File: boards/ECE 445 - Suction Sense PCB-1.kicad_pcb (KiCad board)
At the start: 2 copper layers, 23 parts, among them J1 Paddle Sensor, J2 Motion Sensor, U1 ESP32-WROOM-32E, U2 TPS2120YFPR, U3 AP62150Z6

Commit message: routed
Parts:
- added J3: Battery Connector, Connector_PinSocket_2.00mm:PinSocket_1x02_P2.00mm_Vertical, F.Cu at (182.8, 126.4)
- added J4: Barrel_Jack, Connector_BarrelJack:BarrelJack_CUI_PJ-036AH-SMT_Horizontal, F.Cu at (177.3, 88.1)
- moved H4 85.4 mm to (102.2, 142.4)
- moved H1 72.2 mm to (102.2, 56.3)
- moved C1 67.8 mm to (168.4, 111.6)
- moved C2 65.0 mm to (161.2, 125.9)
- moved C3 63.8 mm to (155.3, 139.6)
- moved H3 54.7 mm to (185.4, 139.8)
- moved C5 32.7 mm to (128.8, 140.0)
- moved H2 24.4 mm to (182.2, 56.0)
- moved R7 23.9 mm to (122.7, 96.0)
- moved J1 19.6 mm to (103.1, 107.1)
- moved U2 18.5 mm to (152.6, 99.6)
- moved U1 14.7 mm to (143.9, 83.5)
- moved J2 13.1 mm to (108.7, 121.2)
- moved C4 12.7 mm to (106.9, 90.4)
- moved R3 12.0 mm to (122.6, 111.1)
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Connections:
- R7 pad 1: +12V -> +12VA
- U2 pad B1: +12V -> +12VA
- U2 pad B3: +12V -> +12VB
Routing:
- net GND: track 0.00 -> 288.4 mm, vias 0 -> 1
- net /3v3: track 0.00 -> 138.7 mm, vias 0 -> 2
- net +12VA: track 0.00 -> 84.3 mm, vias 0 -> 2
- net /EN: track 0.00 -> 82.2 mm, vias 0 -> 4
- net /IO35: track 0.00 -> 75.1 mm, vias 0 -> 2
- net /IO5: track 0.00 -> 55.6 mm, vias 0 -> 1
- net /IO12: track 0.00 -> 47.0 mm, vias 0 -> 1
- net Net-(U3-FB): track 0.00 -> 35.0 mm, vias 0 -> 2
- net Net-(R7-Pad2): track 0.00 -> 34.3 mm
- net Net-(U3-BST): track 0.00 -> 33.1 mm, vias 0 -> 2
- net Net-(R1-Pad2): track 0.00 -> 33.0 mm
- net /BUCK_IN: track 0.00 -> 31.1 mm
- net Net-(U3-SW): track 0.00 -> 29.1 mm, vias 0 -> 2
- net +12VB: track 0.00 -> 18.0 mm, vias 0 -> 1

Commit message: adding changes to the pcb finishing connections with power mux
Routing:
- net GND: track 288.4 -> 318.3 mm, vias 1 -> 3
- net /BUCK_IN: track 31.1 -> 58.8 mm, vias 0 -> 1
- net +12VB: track 18.0 -> 36.4 mm
- net +12VA: track 84.3 -> 93.1 mm
- net /IO2: track 0.00 -> 7.30 mm
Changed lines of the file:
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@@
 	(segment
 		(start 144.5483 112.9453)
-		(end 144.5483 122.1517)
+		(end 144.5483 115.3)
 		(width 0.2)
 		(layer "F.Cu")
@@
 	)
 	(segment
+		(start 144.5483 115.3)
+		(end 144.5483 122.1517)
+		(width 0.2)
+		(layer "F.Cu")
+		(net 2)
+	)
+	(segment
 		(start 173.9937 123.9503)
 		(end 158.371 139.573)
@@
 	)
 	(segment
+		(start 157.7 108.3)
+		(end 157.7 104.943997)
+		(width 0.2)
+		(layer "F.Cu")
+		(net 2)
+	)
+	(segment
+		(start 144.5483 115.3)
+		(end 144.6096 115.3)
+		(width 0.2)
+		(layer "F.Cu")
+		(net 2)
+	)
+	(segment
 		(start 150.8386 75.2141)
 		(end 151.5653 75.2141)
@@
 	)
 	(segment
+		(start 157.7 104.943997)
+		(end 153.178002 100.421999)
+		(width 0.2)
+		(layer "F.Cu")
+		(net 2)
+	)
+	(segment
 		(start 109.984 90.424)
 		(end 105.664 94.744)
@@
 		(net 2)
 	)
+	(via
+		(at 144.6096 115.3)
+		(size 0.6)
+		(drill 0.3)
+		(layers "F.Cu" "B.Cu")
+		(net 2)
+	)
+	(via
+		(at 157.7 108.3)
+		(size 0.6)
+		(drill 0.3)
+		(layers "F.Cu" "B.Cu")
+		(net 2)
+	)
 	(segment
 		(start 144.9615 84.8285)
@@
 	)
 	(segment
+		(start 150.1 115.3)
+		(end 150.1 110.6)
+		(width 0.2)
+		(layer "B.Cu")
+		(net 2)
+	)
+	(segment
 		(start 141.667 82.934)
 		(end 143.067 82.934)
@@
 	)
 	(segment
+		(start 157.7 110.6)
+		(end 157.7 108.3)
+		(width 0.2)
+		(layer "B.Cu")
+		(net 2)
+	)
+	(segment
 		(start 143.067 81.534)
 		(end 141.667 81.534)
@@
 	)
 	(segment
+		(start 144.6096 115.3)
+		(end 150.1 115.3)
+		(width 0.2)
+		(layer "B.Cu")
+		(net 2)
+	)
+	(segment
+		(start 150.1 110.6)
+		(end 157.7 110.6)
+		(width 0.2)
+		(layer "B.Cu")
+		(net 2)
+	)
+	(segment
 		(start 143.767 83.634)
 		(end 144.9615 84.8285)
@@
 	(segment
 		(start 145.2096 132.5116)
-		(end 145.2096 112.197)
+		(end 145.2096 116.7)
 		(width 0.2)
 		(layer "F.Cu")
@@
 	)
 	(segment
+		(start 151.7 110.6)
+		(end 151.7 106.8827)
+		(width 0.2)
+		(layer "F.Cu")
+		(net 5)
+	)
+	(segment
+		(start 145.2096 116.7)
+		(end 152.6 116.7)
+		(width 0.2)
+		(layer "F.Cu")
+		(net 5)
+	)
+	(segment
+		(start 155.2 114.1)
+		(end 151.7 110.6)
+		(width 0.2)
+		(layer "F.Cu")
+		(net 5)
+	)
+	(segment
+		(start 152.6 116.7)
+		(end 155.2 114.1)
+		(width 0.2)
+		(layer "F.Cu")
+		(net 5)
+	)
+	(segment
 		(start 144.9076 111.895)
 		(end 144.498 111.895)
@@
 	)
 	(segment
+		(start 145.2096 116.7)
+		(end 145.2096 112.197)
+		(width 0.2)
+		(layer "F.Cu")
+		(net 5)
+	)
+	(via
+		(at 151.7 106.8827)
+		(size 0.6)
+		(drill 0.3)
+		(layers "F.Cu" "B.Cu")
+		(net 5)
+	)
+	(segment
+		(start 152.801 100.001)
+		(end 152.4 99.6)
+		(width 0.2)
+		(layer "B.Cu")
+		(net 5)
+	)
+	(segment
+		(start 151.7 106.8827)
+		(end 152.801 105.7817)
+		(width 0.2)
+		(layer "B.Cu")
+		(net 5)
+	)
+	(segment
+		(start 152.801 105.7817)
+		(end 152.801 100.001)
+		(width 0.2)
+		(layer "B.Cu")
+		(net 5)
+	)
+	(segment
 		(start 136.5264 113.3083)
 		(end 132.3945 109.1764)
@@
 	)
 	(segment
+		(start 150.8 107.4827)
+		(end 128.3748 107.4827)
+		(width 0.2)
+		(layer "B.Cu")
+		(net 12)
+	)
+	(segment
 		(start 168.4021 110.89)
 		(end 167.3517 111.9404)
@@
 	(segment
 		(start 162.894 107.4827)
-		(end 128.3748 107.4827)
+		(end 150.8 107.4827)
 		(width 0.2)
 		(layer "B.Cu")
@@
 	)
 	(segment
+		(start 152 99.2)
+		(end 150.8 100.4)
+		(width 0.2)
+		(layer "B.Cu")
+		(net 12)
+	)
+	(segment
 		(start 182.753 126.365)
 		(end 181.7763 126.365)
@@
 	)
 	(segment
+		(start 150.8 100.4)
+		(end 150.8 107.4827)
+		(width 0.2)
+		(layer "B.Cu")
+		(net 12)
+	)
+	(segment
 		(start 146.3114 112.395)
 		(end 145.923 112.395)
@@
 	)
 	(segment
+		(start 153.178002 96.565002)
+		(end 153.178002 98.789998)
+		(width 0.2)
+		(layer "F.Cu")
+		(net 38)
+	)
+	(segment
+		(start 149.587 92.974)
+		(end 153.178002 96.565002)
+		(width 0.2)
+		(layer "F.Cu")
+		(net 38)
+	)
+	(segment
 		(start 183.3504 91.1795)
 		(end 183.092 90.9211)
@@
 	)
 	(segment
-		(start 181.1959 93.334)
-		(end 168.7124 93.334)
+		(start 181.2299 93.3)
+		(end 168.7464 93.3)
 		(width 0.2)
 		(layer "B.Cu")
@@
 	(segment
 		(start 183.3504 91.1795)
-		(end 181.1959 93.334)
-		(width 0.2)
-		(layer "B.Cu")
+		(end 181.2299 93.3)
+		(width 0.2)
+		(layer "B.Cu")
+		(net 59)
+	)
+	(segment
+		(start 168.7464 93.3)
+		(end 162.8464 99.2)
+		(width 0.2)
+		(layer "B.Cu")
+		(net 59)
+	)
+	(segment
+		(start 162.8464 99.2)
+		(end 152.7 99.2)
+		(width 0.2)
+		(layer "B.Cu")

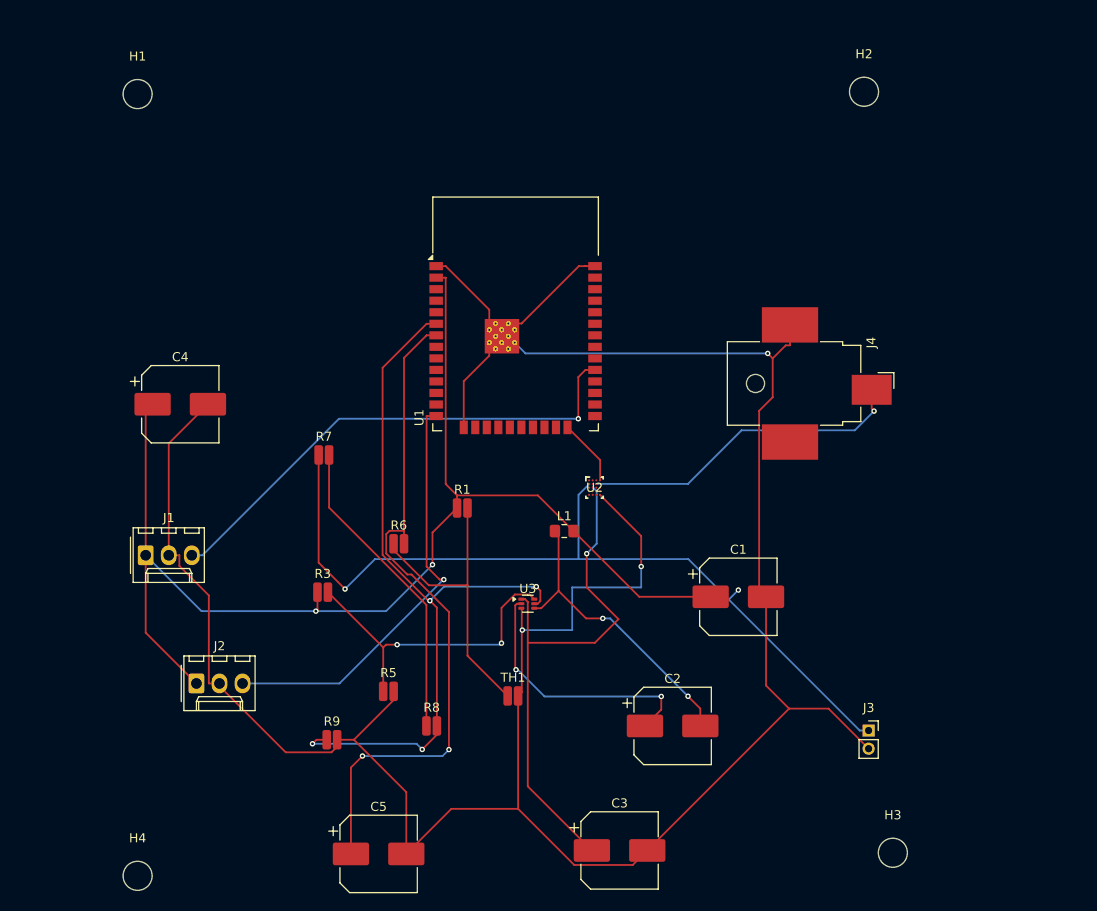
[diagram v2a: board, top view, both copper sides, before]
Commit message: finsih adding charging
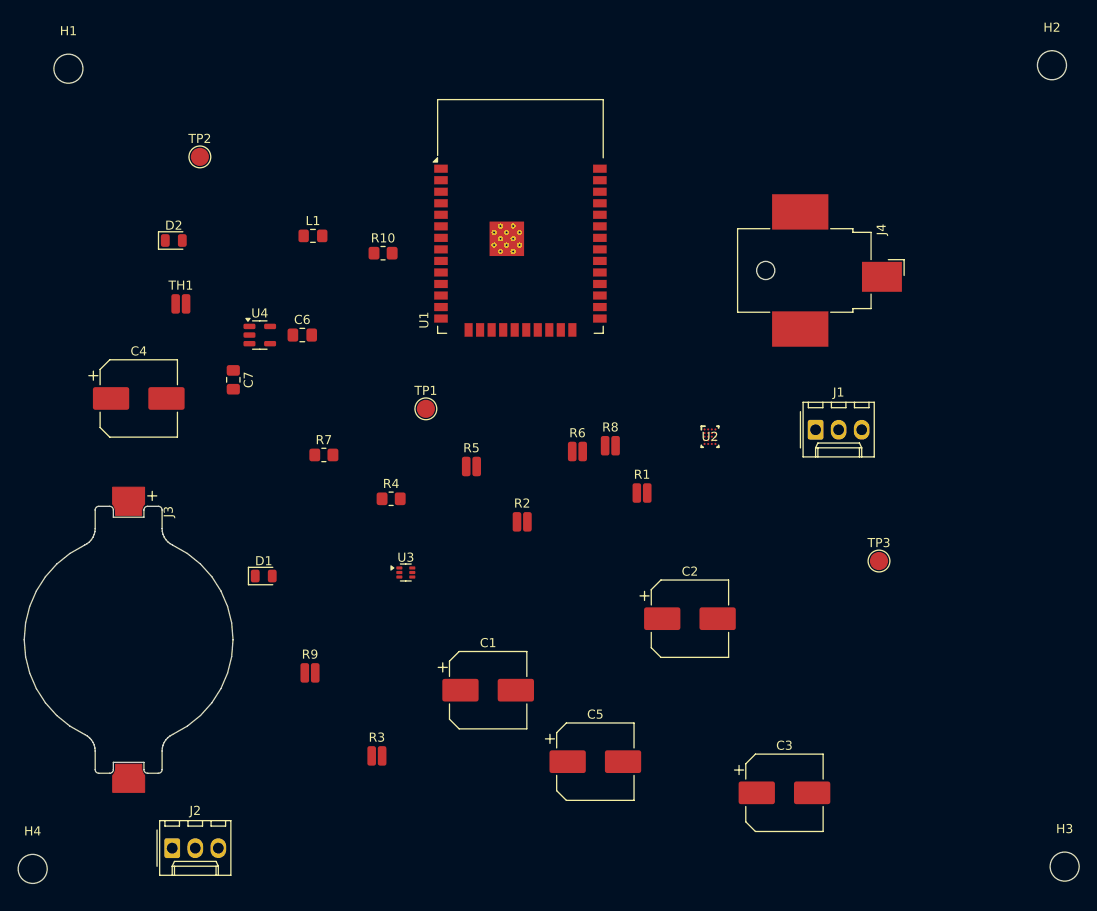
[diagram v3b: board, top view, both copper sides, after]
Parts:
- added C6: 4.7uF, Capacitor_SMD:C_0805_2012Metric_Pad1.18x1.45mm_HandSolder, F.Cu at (120.4, 82.8)
- added C7: 4.7uF, Capacitor_SMD:C_0805_2012Metric_Pad1.18x1.45mm_HandSolder, F.Cu at (112.8, 87.7)
- added D1: LED_Small, LED_SMD:LED_0805_2012Metric, F.Cu at (116.1, 109.3)
- added D2: LED_Small, LED_SMD:LED_0805_2012Metric, F.Cu at (106.2, 72.4)
- added R10: 850, Resistor_SMD:R_0805_2012Metric_Pad1.20x1.40mm_HandSolder, F.Cu at (129.3, 73.8)
- added R2: 1.5K, Resistor_SMD:R_0508_1220Metric, F.Cu at (144.6, 103.4)
- added R4: 850, Resistor_SMD:R_0805_2012Metric_Pad1.20x1.40mm_HandSolder, F.Cu at (130.2, 100.8)
- added TP1: 3.7+, TestPoint:TestPoint_Pad_D2.0mm, F.Cu at (134.0, 90.9)
- added TP2: 3v3, TestPoint:TestPoint_Pad_D2.0mm, F.Cu at (109.1, 63.2)
- added TP3: BUCK_IN, TestPoint:TestPoint_Pad_D2.0mm, F.Cu at (183.9, 107.7)
- added U4: MCP73831-2-OT, Package_TO_SOT_SMD:SOT-23-5, F.Cu at (115.7, 82.8)
- C3: value C -> 440uf
- J3: footprint Connector_PinSocket_2.00mm:PinSocket_1x02_P2.00mm_Vertical -> Battery:BatteryHolder_Keystone_1057_1x2032
- R3: value 52.3k -> 5.1K
- R5: value 10k -> 2.2K
- R7: value 2.2K -> 120k; footprint Resistor_SMD:R_0508_1220Metric -> Resistor_SMD:R_0805_2012Metric_Pad1.20x1.40mm_HandSolder
- R8: value 2.2K -> 1.5K
- R9: value 1.5K -> 5.1K
- moved J3 82.1 mm to (101.2, 116.4), turned to -90 degrees
- moved J1 75.1 mm to (176.9, 93.2)
- moved TH1 56.6 mm to (107.0, 79.4)
- moved L1 42.7 mm to (121.5, 71.9)
- moved R8 36.6 mm to (154.3, 95.0)
- moved C1 29.4 mm to (140.8, 121.9)
- moved R5 26.4 mm to (139.0, 97.3)
- moved C5 25.9 mm to (152.7, 129.8)
- moved R6 22.1 mm to (150.7, 95.6)
- moved H2 20.9 mm to (202.9, 53.1)
- moved R1 19.9 mm to (157.8, 100.2)
- moved C3 19.2 mm to (173.5, 133.2)
- moved R3 19.0 mm to (128.6, 129.2)
- moved H3 19.0 mm to (204.3, 141.4)
- moved J2 18.3 mm to (106.0, 139.3)
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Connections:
- net +12VB renamed +5VB
- J3 pad 1: +12VA -> +3.7VA
- R3 pad 2: Net-(U3-FB) -> Net-(R2-Pad1)
- R7 pad 1: +12VA -> Net-(U4-PROG)
- R7 pad 2: Net-(R7-Pad2) -> Net-(U4-V_{SS})
- R8 pad 1: Net-(R7-Pad2) -> +3.7VA
- U2 pad B1: +12VA -> +3.7VA
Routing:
- net GND: track 318.3 -> 0.00 mm, vias 3 -> 0
- net /3v3: track 138.7 -> 0.00 mm, vias 2 -> 0
- net +12VA: track 93.1 -> 0.00 mm, vias 2 -> 0
- net /EN: track 82.2 -> 0.00 mm, vias 4 -> 0
- net /IO35: track 75.1 -> 0.00 mm, vias 2 -> 0
- net /BUCK_IN: track 58.8 -> 0.00 mm, vias 1 -> 0
- net /IO5: track 55.6 -> 0.00 mm, vias 1 -> 0
- net /IO12: track 47.0 -> 0.00 mm, vias 1 -> 0
- net +5VB: track 36.4 -> 0.00 mm, vias 1 -> 0
- net Net-(U3-FB): track 35.0 -> 0.00 mm, vias 2 -> 0
- net Net-(R7-Pad2): track 34.3 -> 0.00 mm
- net Net-(U3-BST): track 33.1 -> 0.00 mm, vias 2 -> 0
- net Net-(R1-Pad2): track 33.0 -> 0.00 mm
- net Net-(U3-SW): track 29.1 -> 0.00 mm, vias 2 -> 0
- net /IO2: track 7.30 -> 0.00 mm
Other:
- board outline added: 23 x 29.4 mm

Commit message: adding changes to the journal and pcb design, as well as adding the LED gnd connection on schematic
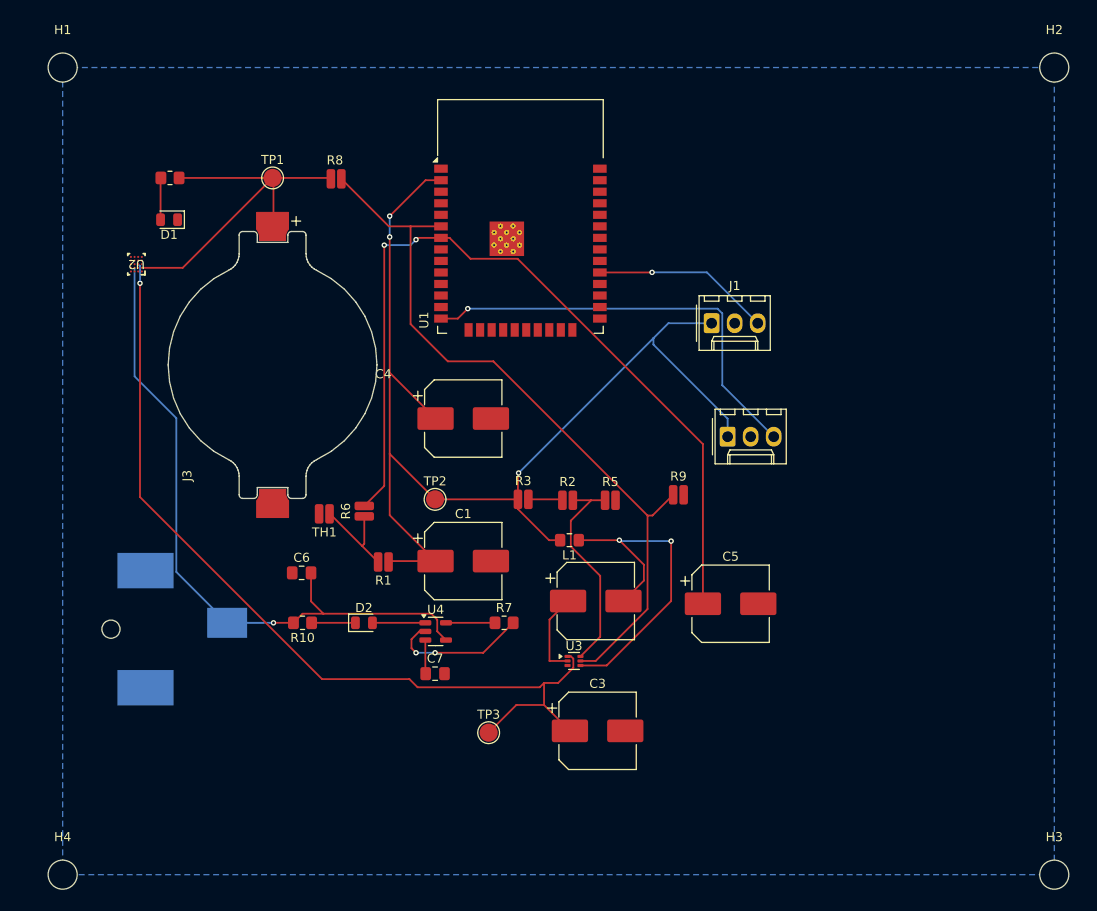
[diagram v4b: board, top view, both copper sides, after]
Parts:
- J4: moved to B.Cu
- moved J4 82.2 mm to (106.3, 115.2), turned to 90 degrees
- moved J2 76.1 mm to (167.2, 94.0)
- moved U2 66.0 mm to (102.1, 75.0), turned to 180 degrees
- moved D2 47.0 mm to (127.2, 114.5)
- moved TP3 47.0 mm to (140.9, 126.6)
- moved TP2 45.8 mm to (135.0, 100.9)
- moved R9 45.1 mm to (161.8, 100.4)
- moved L1 43.8 mm to (149.8, 105.4), turned to 180 degrees
- moved R4 42.9 mm to (105.8, 65.5)
- moved R8 42.1 mm to (124.1, 65.6)
- moved R10 41.7 mm to (120.4, 114.5), turned to 180 degrees
- moved D1 40.6 mm to (105.7, 70.1), turned to 180 degrees
- moved C7 39.3 mm to (135.0, 120.1), turned to 0 degrees
- moved U4 38.0 mm to (135.1, 115.5)
- moved C4 35.8 mm to (138.1, 92.0)
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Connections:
- D1 pad 1: unconnected-(D1-K-Pad1) -> GND
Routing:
- net /3v3: track 0.00 -> 128.3 mm, vias 0 -> 3
- net /BUCK_IN: track 0.00 -> 98.6 mm, vias 0 -> 1
- net /IO35: track 0.00 -> 92.1 mm, vias 0 -> 2
- net /EN: track 0.00 -> 82.6 mm
- net +5VB: track 0.00 -> 74.8 mm, vias 0 -> 1
- net /IO12: track 0.00 -> 47.6 mm, vias 0 -> 1
- net +3.7VA: track 0.00 -> 41.1 mm
- net Net-(U3-BST): track 0.00 -> 38.5 mm, vias 0 -> 2
- net Net-(U3-FB): track 0.00 -> 23.9 mm
- net /IO5: track 0.00 -> 19.7 mm, vias 0 -> 1
- net Net-(U4-V_{SS}): track 0.00 -> 15.6 mm, vias 0 -> 2
- net Net-(R1-Pad2): track 0.00 -> 10.9 mm
- net Net-(U3-SW): track 0.00 -> 9.44 mm
- net Net-(D2-A): track 0.00 -> 5.83 mm
- net Net-(U4-PROG): track 0.00 -> 5.40 mm
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- added copper zone on B.Cu, net GND

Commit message: adding changes need to update pcb with new package
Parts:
- moved H3 25.7 mm to (179.1, 133.3)
- moved H2 24.1 mm to (179.1, 53.3)
- moved H4 8.89 mm to (94.0, 133.3)
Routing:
- net /IO2: track 0.00 -> 62.2 mm, vias 0 -> 1
- net GND: track 0.00 -> 37.1 mm, vias 0 -> 7
- net +5VB: track 74.8 -> 62.8 mm
- net (no net): track 0.00 -> 3.59 mm, vias 0 -> 2
- net /BUCK_IN: track 98.6 -> 96.4 mm
- added copper zone on F.Cu, net GND
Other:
- board size 23 x 29.4 mm -> 92.7 x 88.9 mm
